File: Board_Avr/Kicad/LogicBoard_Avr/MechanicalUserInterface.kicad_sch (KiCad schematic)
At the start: 12 parts, among them J1 I2C_Interface, J2 UART_Interface, J3 MechanicalUserInterfaceConnec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, U2 TLP291

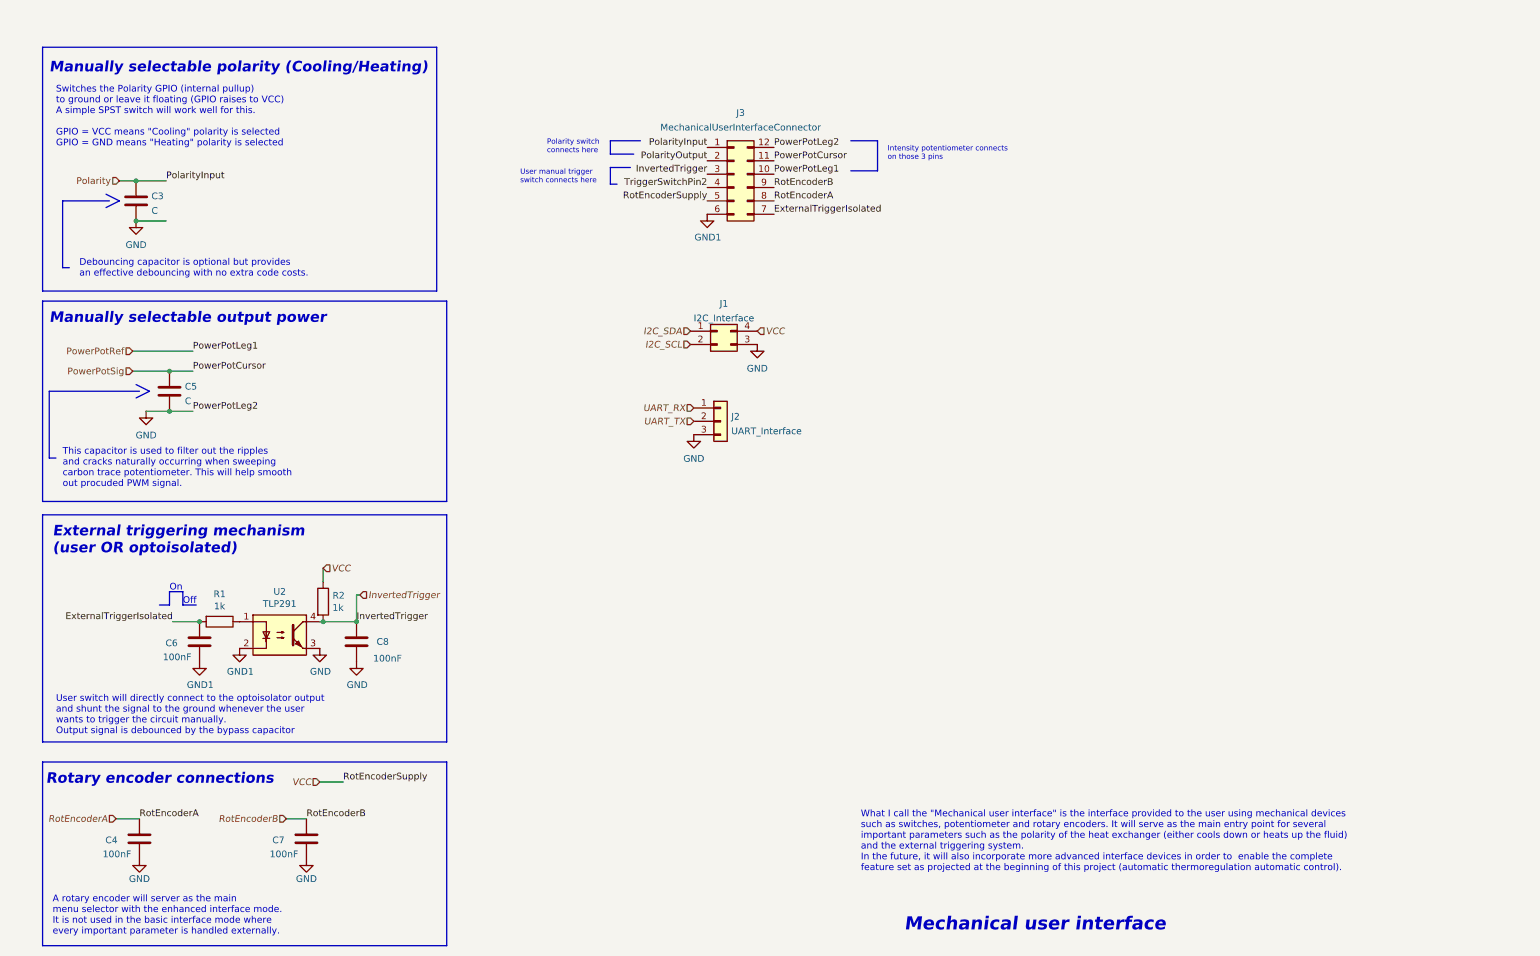
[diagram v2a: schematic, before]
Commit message: Added several external connections and reworked leds and output signals
Signed-off-by: bebenlebricolo <benoittarrade@hotmail.fr>
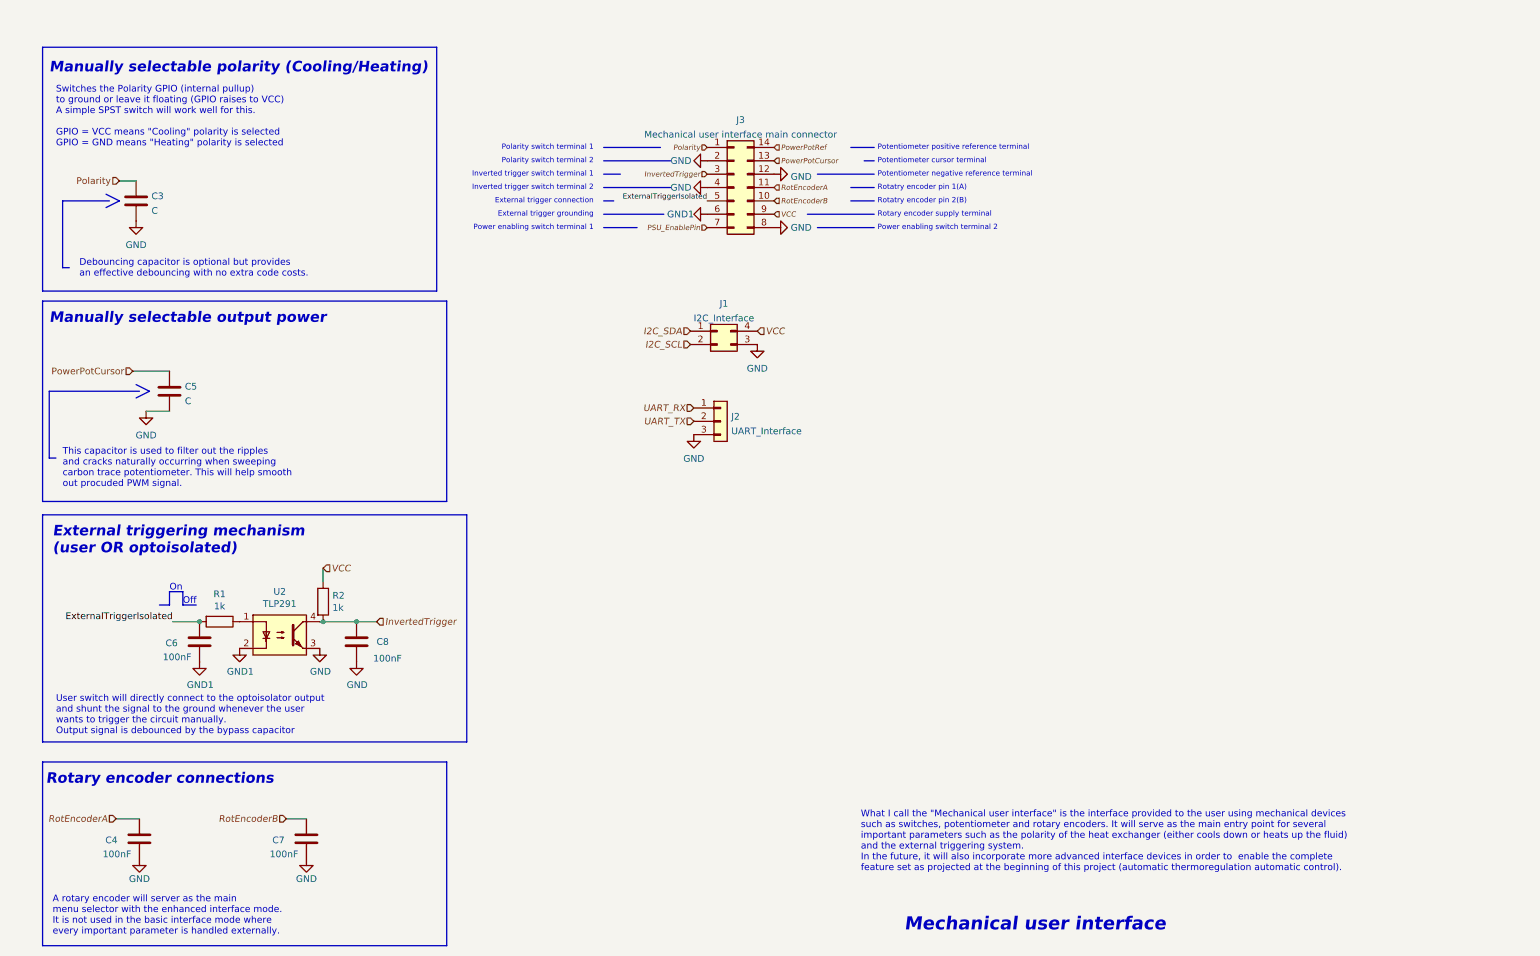
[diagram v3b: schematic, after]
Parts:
- removed J3: MechanicalUserInterfaceConnector, symbol Connector_Generic:Conn_02x06_Counter_Clockwise
- added J3: Mechanical user interface main connector, symbol Connector_Generic:Conn_02x07_Counter_Clockwise
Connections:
- net ExternalTriggerIsolated: now also J3.5 (Pin_5)
- net GND: now also J3.12 (Pin_12), J3.2 (Pin_2), J3.4 (Pin_4), J3.8 (Pin_8)
- net GND1: now also J3.6 (Pin_6)
- net InvertedTrigger: now also J3.3 (Pin_3)
- net Polarity: now also J3.1 (Pin_1)
- net PowerPotRef: now also J3.14 (Pin_14)
- net RotEncoderA: now also J3.11 (Pin_11)
- net RotEncoderB: now also J3.10 (Pin_10)
- net VCC: now also J3.9 (Pin_9)
- net PowerPotSig renamed PowerPotCursor
- net PowerPotCursor: now also J3.13 (Pin_13)
- new net PSU_EnablePin: J3.7 (Pin_7)
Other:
- note added: "External trigger connection"
- note added: "External trigger grounding"
- note added: "Inverted trigger switch terminal 1"
- note added: "Inverted trigger switch terminal 2"
- note added: "Polarity switch terminal 1"
- note added: "Polarity switch terminal 2"
- note added: "Potentiometer cursor terminal"
- note added: "Potentiometer negative reference terminal"
- note added: "Potentiometer positive reference terminal"
- note added: "Power enabling switch terminal 1"
- note added: "Power enabling switch terminal 2"
- note added: "Rotary encoder supply terminal"
- note added: "Rotatry encoder pin 1(A)"
- note added: "Rotatry encoder pin 2(B)"
- note removed: "Intensity potentiometer connects on those 3 pins"
- note removed: "Polarity switch connects here"
- note removed: "User manual trigger switch connects here"

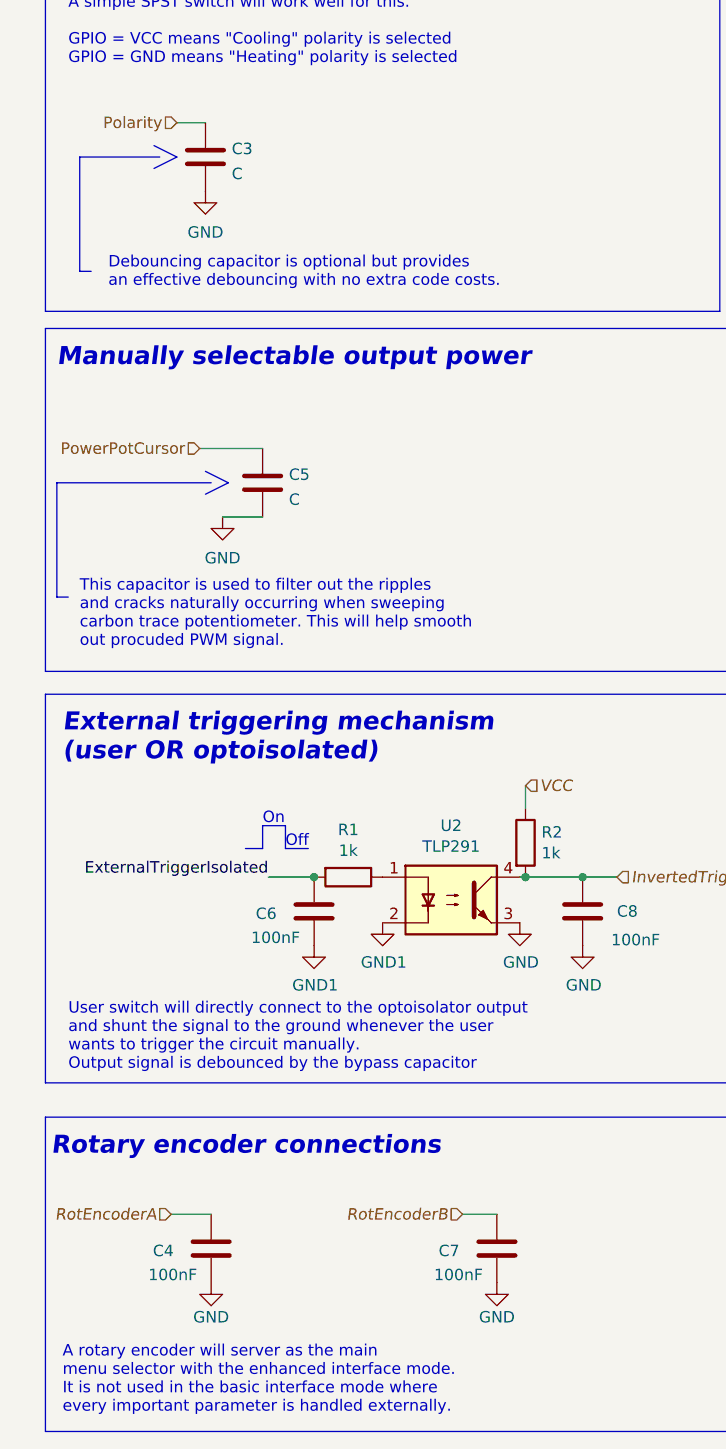
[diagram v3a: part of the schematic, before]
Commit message: Started routing all traces
Signed-off-by: bebenlebricolo <benoittarrade@hotmail.fr>
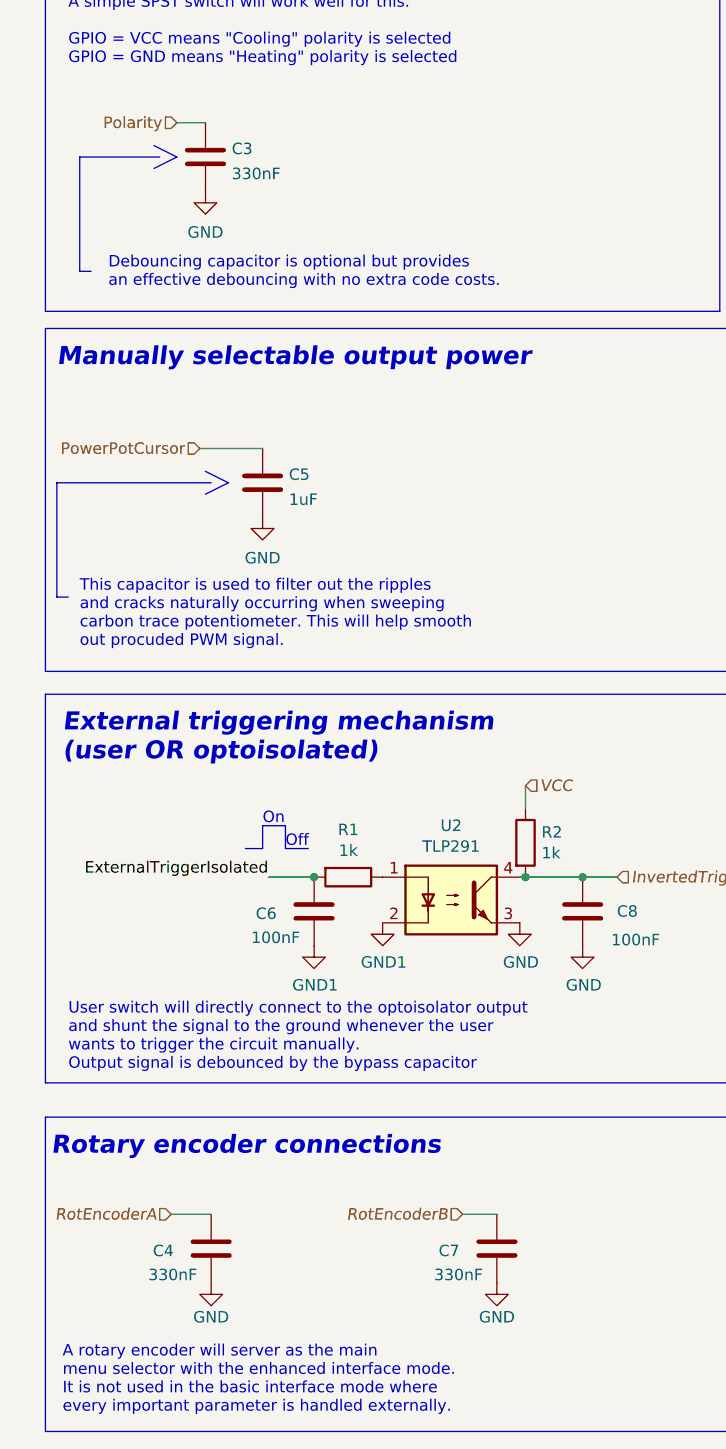
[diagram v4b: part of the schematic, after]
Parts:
- C3: value C -> 330nF; footprint (none) -> Capacitor_SMD:C_1206_3216Metric
- C4, C7: value 100nF -> 330nF; footprint Capacitor_SMD:C_1206_3216Metric_Pad1.33x1.80mm_HandSolder -> Capacitor_SMD:C_1206_3216Metric
- C5: value C -> 1uF; footprint (none) -> Capacitor_SMD:C_1206_3216Metric
- C6, C8: footprint Capacitor_SMD:C_1206_3216Metric_Pad1.33x1.80mm_HandSolder -> Capacitor_SMD:C_1206_3216Metric
- J1: footprint (none) -> Connector_PinHeader_2.54mm:PinHeader_2x02_P2.54mm_Vertical
- J2: footprint (none) -> Connector_PinHeader_2.54mm:PinHeader_1x03_P2.54mm_Vertical
- J3: footprint (none) -> Connector_PinHeader_2.54mm:PinHeader_2x07_P2.54mm_Vertical
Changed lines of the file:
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@@
-    (stroke (width 0) (type default) (color 0 0 0 0))
-  )
-  (wire (pts (xy 42.545 92.71) (xy 46.99 92.71))
     (stroke (width 0) (type default) (color 0 0 0 0))
   )
@@
     (property "Reference" "J3" (id 0) (at 155.575 37.3085 0))
     (property "Value" "Mechanical user interface main connector" (id 1) (at 155.575 40.0836 0))
-    (property "Footprint" "" (id 2) (at 154.305 50.165 0)
+    (property "Footprint" "Connector_PinHeader_2.54mm:PinHeader_2x07_P2.54mm_Vertical" (id 2) (at 154.305 50.165 0)
       (effects (font (size 1.27 1.27)) hide)
     )
@@
       (effects (font (size 1.27 1.27)) (justify left))
     )
-    (property "Value" "C" (id 1) (at 49.911 90.7666 0)
-      (effects (font (size 1.27 1.27)) (justify left))
-    )
-    (property "Footprint" "" (id 2) (at 47.9552 92.71 0)
+    (property "Value" "1uF" (id 1) (at 49.911 90.7666 0)
+      (effects (font (size 1.27 1.27)) (justify left))
+    )
+    (property "Footprint" "Capacitor_SMD:C_1206_3216Metric" (id 2) (at 47.9552 92.71 0)
       (effects (font (size 1.27 1.27)) hide)
     )
@@
     (pin "1")
   )
-  (symbol (lib_id "power:GND") (at 42.545 92.71 0) (unit 1)
-    (in_bom yes) (on_board yes) (fields_autoplaced)
-    (property "Reference" "#PWR0113" (id 0) (at 42.545 99.06 0)
-      (effects (font (size 1.27 1.27)) hide)
-    )
-    (property "Value" "GND" (id 1) (at 42.545 97.2725 0))
-    (property "Footprint" "" (id 2) (at 42.545 92.71 0)
-      (effects (font (size 1.27 1.27)) hide)
-    )
-    (property "Datasheet" "" (id 3) (at 42.545 92.71 0)
+  (symbol (lib_id "power:GND") (at 46.99 92.71 0) (unit 1)
+    (in_bom yes) (on_board yes) (fields_autoplaced)
+    (property "Reference" "#PWR0113" (id 0) (at 46.99 99.06 0)
+      (effects (font (size 1.27 1.27)) hide)
+    )
+    (property "Value" "GND" (id 1) (at 46.99 97.2725 0))
+    (property "Footprint" "" (id 2) (at 46.99 92.71 0)
+      (effects (font (size 1.27 1.27)) hide)
+    )
+    (property "Datasheet" "" (id 3) (at 46.99 92.71 0)
       (effects (font (size 1.27 1.27)) hide)
     )
@@
       (effects (font (size 1.27 1.27)) (justify right))
     )
-    (property "Footprint" "Capacitor_SMD:C_1206_3216Metric_Pad1.33x1.80mm_HandSolder" (id 2) (at 51.7398 132.715 0)
+    (property "Footprint" "Capacitor_SMD:C_1206_3216Metric" (id 2) (at 51.7398 132.715 0)
       (effects (font (size 1.27 1.27)) hide)
     )
@@
       (effects (font (size 1.27 1.27)) (justify right))
     )
-    (property "Value" "100nF" (id 1) (at 34.29 176.911 0)
-      (effects (font (size 1.27 1.27)) (justify right))
-    )
-    (property "Footprint" "Capacitor_SMD:C_1206_3216Metric_Pad1.33x1.80mm_HandSolder" (id 2) (at 40.3098 170.18 0)
+    (property "Value" "330nF" (id 1) (at 34.29 176.911 0)
+      (effects (font (size 1.27 1.27)) (justify right))
+    )
+    (property "Footprint" "Capacitor_SMD:C_1206_3216Metric" (id 2) (at 40.3098 170.18 0)
       (effects (font (size 1.27 1.27)) hide)
     )
@@
       (effects (font (size 1.27 1.27)) (justify right))
     )
-    (property "Value" "100nF" (id 1) (at 66.04 176.911 0)
-      (effects (font (size 1.27 1.27)) (justify right))
-    )
-    (property "Footprint" "Capacitor_SMD:C_1206_3216Metric_Pad1.33x1.80mm_HandSolder" (id 2) (at 72.0598 170.18 0)
+    (property "Value" "330nF" (id 1) (at 66.04 176.911 0)
+      (effects (font (size 1.27 1.27)) (justify right))
+    )
+    (property "Footprint" "Capacitor_SMD:C_1206_3216Metric" (id 2) (at 72.0598 170.18 0)
       (effects (font (size 1.27 1.27)) hide)
     )
@@
       (effects (font (size 1.27 1.27)) (justify right))
     )
-    (property "Footprint" "Capacitor_SMD:C_1206_3216Metric_Pad1.33x1.80mm_HandSolder" (id 2) (at 81.5848 132.715 0)
+    (property "Footprint" "Capacitor_SMD:C_1206_3216Metric" (id 2) (at 81.5848 132.715 0)
       (effects (font (size 1.27 1.27)) hide)
     )
@@
       (effects (font (size 1.27 1.27)) (justify left))
     )
-    (property "Footprint" "" (id 2) (at 151.765 94.615 0)
+    (property "Footprint" "Connector_PinHeader_2.54mm:PinHeader_1x03_P2.54mm_Vertical" (id 2) (at 151.765 94.615 0)
       (effects (font (size 1.27 1.27)) hide)
     )
@@
     (property "Reference" "J1" (id 0) (at 152.4 72.2335 0))
     (property "Value" "I2C_Interface" (id 1) (at 152.4 75.0086 0))
-    (property "Footprint" "" (id 2) (at 151.13 77.47 0)
+    (property "Footprint" "Connector_PinHeader_2.54mm:PinHeader_2x02_P2.54mm_Vertical" (id 2) (at 151.13 77.47 0)
       (effects (font (size 1.27 1.27)) hide)
     )
@@
       (effects (font (size 1.27 1.27)) (justify left))
     )
-    (property "Value" "C" (id 1) (at 43.561 54.5716 0)
-      (effects (font (size 1.27 1.27)) (justify left))
-    )
-    (property "Footprint" "" (id 2) (at 41.6052 56.515 0)
-      (effects (font (size 1.27 1.27)) hide)
-    )
+    (property "Value" "330nF" (id 1) (at 43.561 54.5716 0)
+      (effects (font (size 1.27 1.27)) (justify left))
+    )
+    (property "Footprint" "Capacitor_SMD:C_1206_3216Metric" (id 2) (at 41.6052 56.515 0)
+      (effects (font (size 1.27 1.27)) hide)
+    )
